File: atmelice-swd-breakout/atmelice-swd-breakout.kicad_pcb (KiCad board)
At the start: 2 copper layers, 23.7 x 7.6 mm, 2 parts, among them J1 Conn_02x05_Odd_Even, J2 Conn_01x06

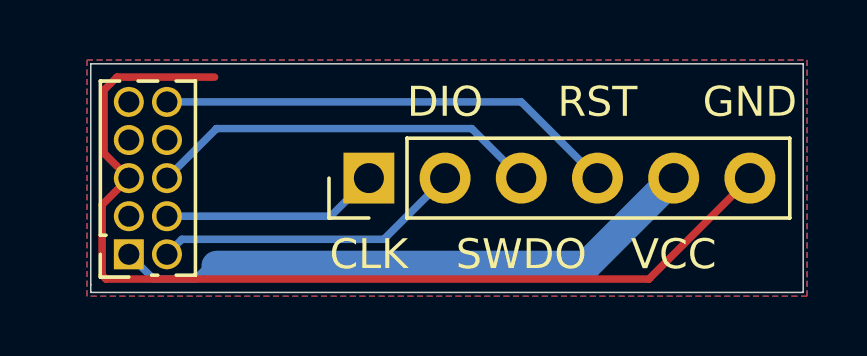
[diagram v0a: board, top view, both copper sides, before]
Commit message: atmelice-swd-breakout: Nov2020 release
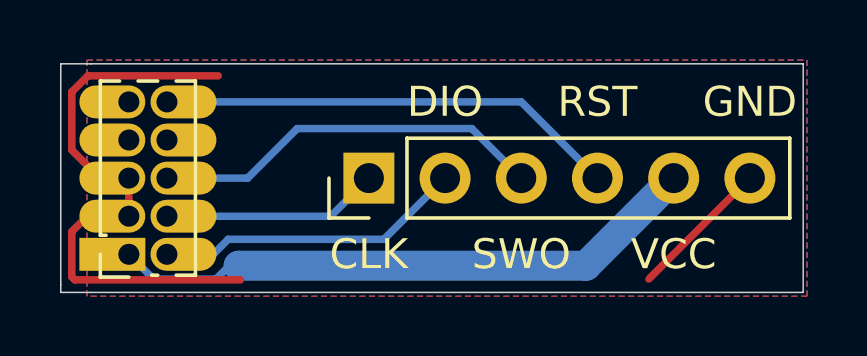
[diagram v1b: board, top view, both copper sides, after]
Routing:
- net /GND: track 33.8 -> 24.6 mm
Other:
- board size 23.7 x 7.6 mm -> 24.7 x 7.6 mm
- net class Default: clearance 0.2 -> 0.127
- rule trace_clearance: 0.2 -> 0.127
- board text added: "SWO"
- board text removed: "SWDO"
